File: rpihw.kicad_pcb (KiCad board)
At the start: 2 copper layers, 207 x 78.7 mm, 101 parts, among them P1 CONN_01X02, P101 CONN_01X02, P102 CONN_01X02, P103 CONN_01X08, P2 CONN_01X02, P3 CONN_02X20, Q1 2N3904BU, Q2 2N3904BU, Q3 2N3904BU, Q4 2N3904BU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

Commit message: Many small improvements.
* Move to V1.1 using less glue logic in the 7-seg display controller.

* Complete perfboard wiring diagram, show in layers.

* Minor spelling error and formatting improvements.
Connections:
- U2 pad 10: Net-(U2-Pad10) -> /SPI 7-SEG DPLY KEYPAD CTL DIP/*RST
- U2 pad 7: Net-(U2-Pad10) -> /SPI 7-SEG DPLY KEYPAD CTL DIP/*RST
- U2 pad 9: Net-(U2-Pad10) -> /SPI 7-SEG DPLY KEYPAD CTL DIP/*RST
- U3 pad 1: Net-(U2-Pad14) -> /SPI 7-SEG DPLY KEYPAD CTL DIP/GND
- U3 pad 10: Net-(U3-Pad10) -> /SPI 7-SEG DPLY KEYPAD CTL DIP/GND
- U3 pad 2: Net-(U2-Pad13) -> /SPI 7-SEG DPLY KEYPAD CTL DIP/GND
- U3 pad 4: Net-(U2-Pad12) -> /SPI 7-SEG DPLY KEYPAD CTL DIP/GND
- U3 pad 5: Net-(U3-Pad3) -> /SPI 7-SEG DPLY KEYPAD CTL DIP/GND
- U3 pad 8: Net-(U2-Pad10) -> Net-(U3-Pad8)
- U3 pad 9: /SPI 7-SEG DPLY KEYPAD CTL DIP/*RST -> /SPI 7-SEG DPLY KEYPAD CTL DIP/GND
- U4 pad 1: Net-(U3-Pad6) -> /SPI 7-SEG DPLY KEYPAD CTL DIP/SS
- U4 pad 2: Net-(U3-Pad10) -> Net-(U4-Pad2)
- U4 pad 3: /SPI 7-SEG DPLY KEYPAD CTL DIP/SS -> /SPI 7-SEG DPLY KEYPAD CTL DIP/GND
- U6 pad 1: Net-(U4-Pad4) -> Net-(U4-Pad2)

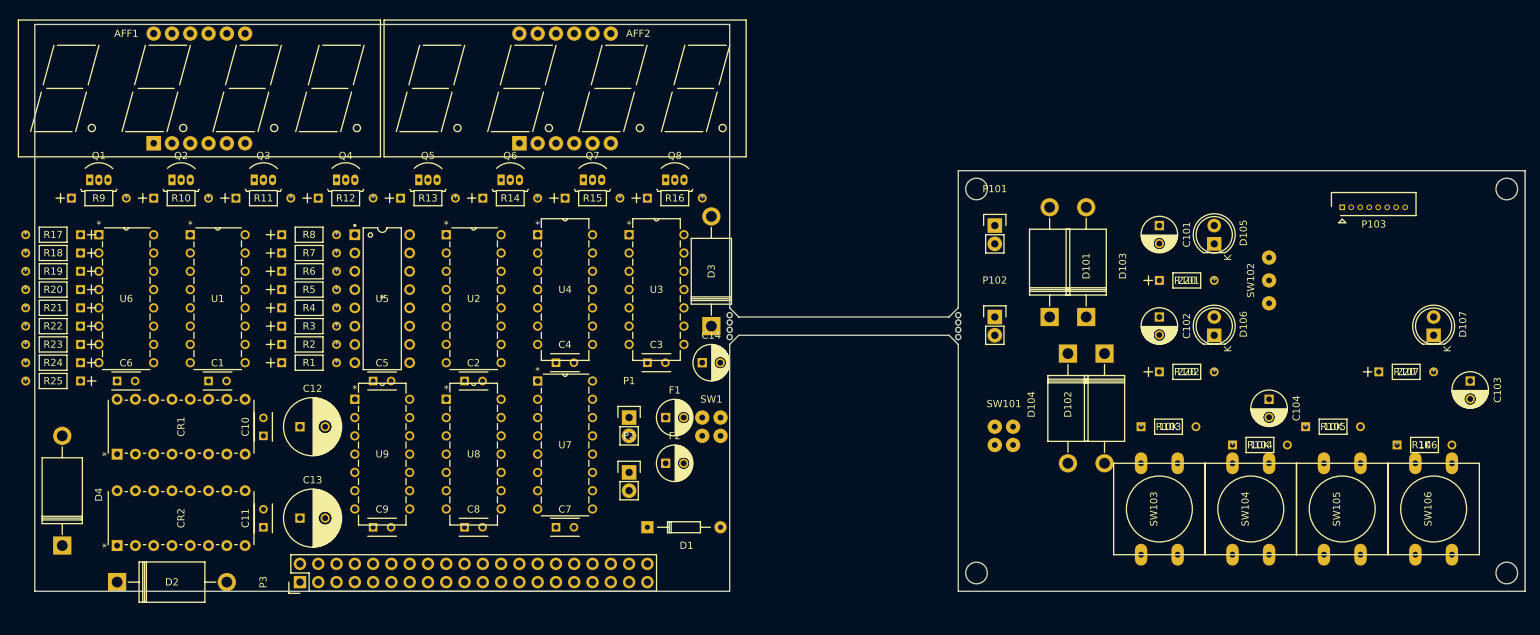
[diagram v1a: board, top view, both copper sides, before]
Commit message: Add auto-routed PCB traces just because we can.
Note that my placeholder switch pad footprints are bad and will need to
be replaced with ones that have the actual numbers for all 4 pins.
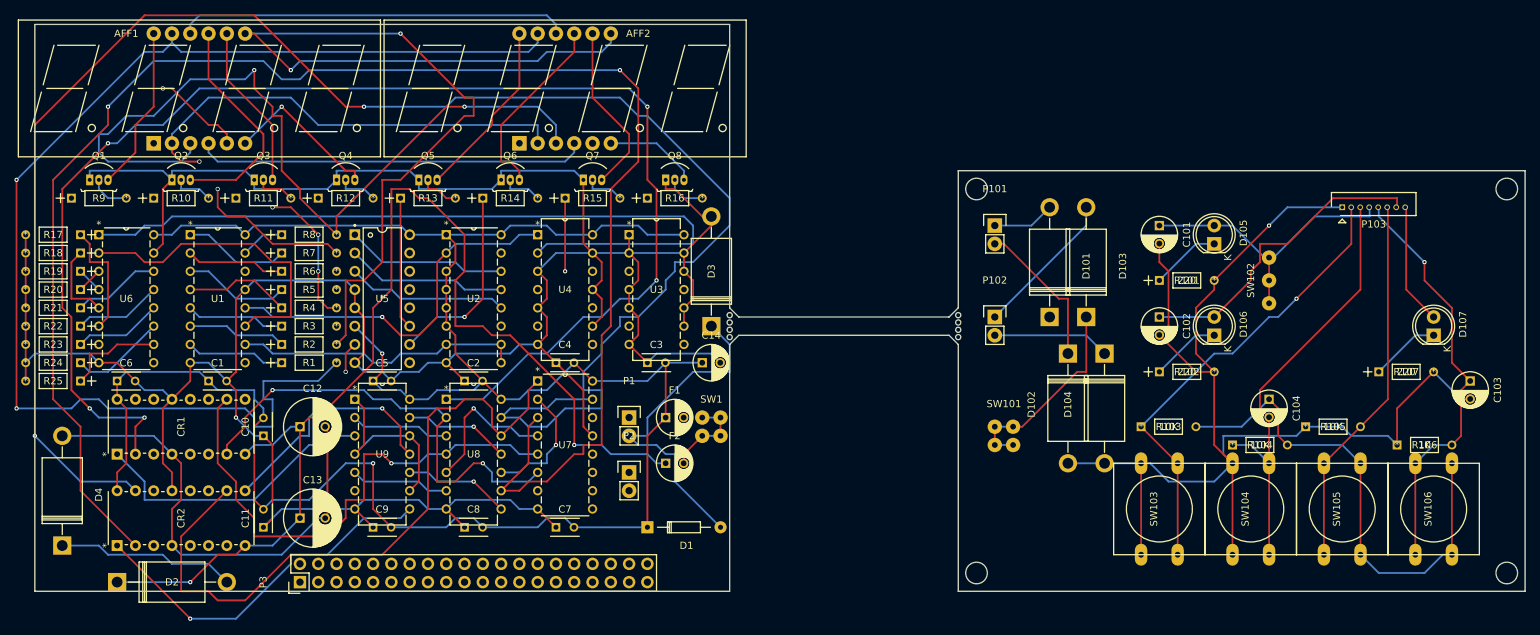
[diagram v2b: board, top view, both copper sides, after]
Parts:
- moved D102 5.08 mm to (196.8, 83.8)
- moved D104 5.08 mm to (201.9, 83.8)
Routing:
- net /SPI 7-SEG DPLY KEYPAD CTL DIP/GND: track 0.00 -> 442.0 mm, vias 0 -> 1
- net /SPI 7-SEG DPLY KEYPAD CTL DIP/VCC: track 0.00 -> 309.3 mm, vias 0 -> 2
- net Net-(CR2-Pad15): track 0.00 -> 247.2 mm, vias 0 -> 2
- net Net-(CR2-Pad2): track 0.00 -> 229.0 mm, vias 0 -> 2
- net Net-(CR1-Pad2): track 0.00 -> 214.8 mm, vias 0 -> 5
- net Net-(AFF1-Pad1): track 0.00 -> 178.8 mm
- net Net-(AFF1-Pad11): track 0.00 -> 174.1 mm, vias 0 -> 2
- net Net-(C101-Pad2): track 0.00 -> 173.5 mm, vias 0 -> 1
- net /SPI MOTOR CTL DIP/VS: track 0.00 -> 156.8 mm, vias 0 -> 2
- net Net-(AFF1-Pad7): track 0.00 -> 137.1 mm, vias 0 -> 2
- net Net-(AFF1-Pad10): track 0.00 -> 128.7 mm
- net Net-(AFF1-Pad4): track 0.00 -> 120.6 mm
- net Net-(AFF1-Pad3): track 0.00 -> 114.1 mm, vias 0 -> 2
- net Net-(AFF1-Pad5): track 0.00 -> 113.2 mm, vias 0 -> 2
- net Net-(U4-Pad2): track 0.00 -> 108.8 mm
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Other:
- copper layers 2 -> 4
